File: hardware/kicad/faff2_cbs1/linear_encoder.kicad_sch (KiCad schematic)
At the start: 0 parts

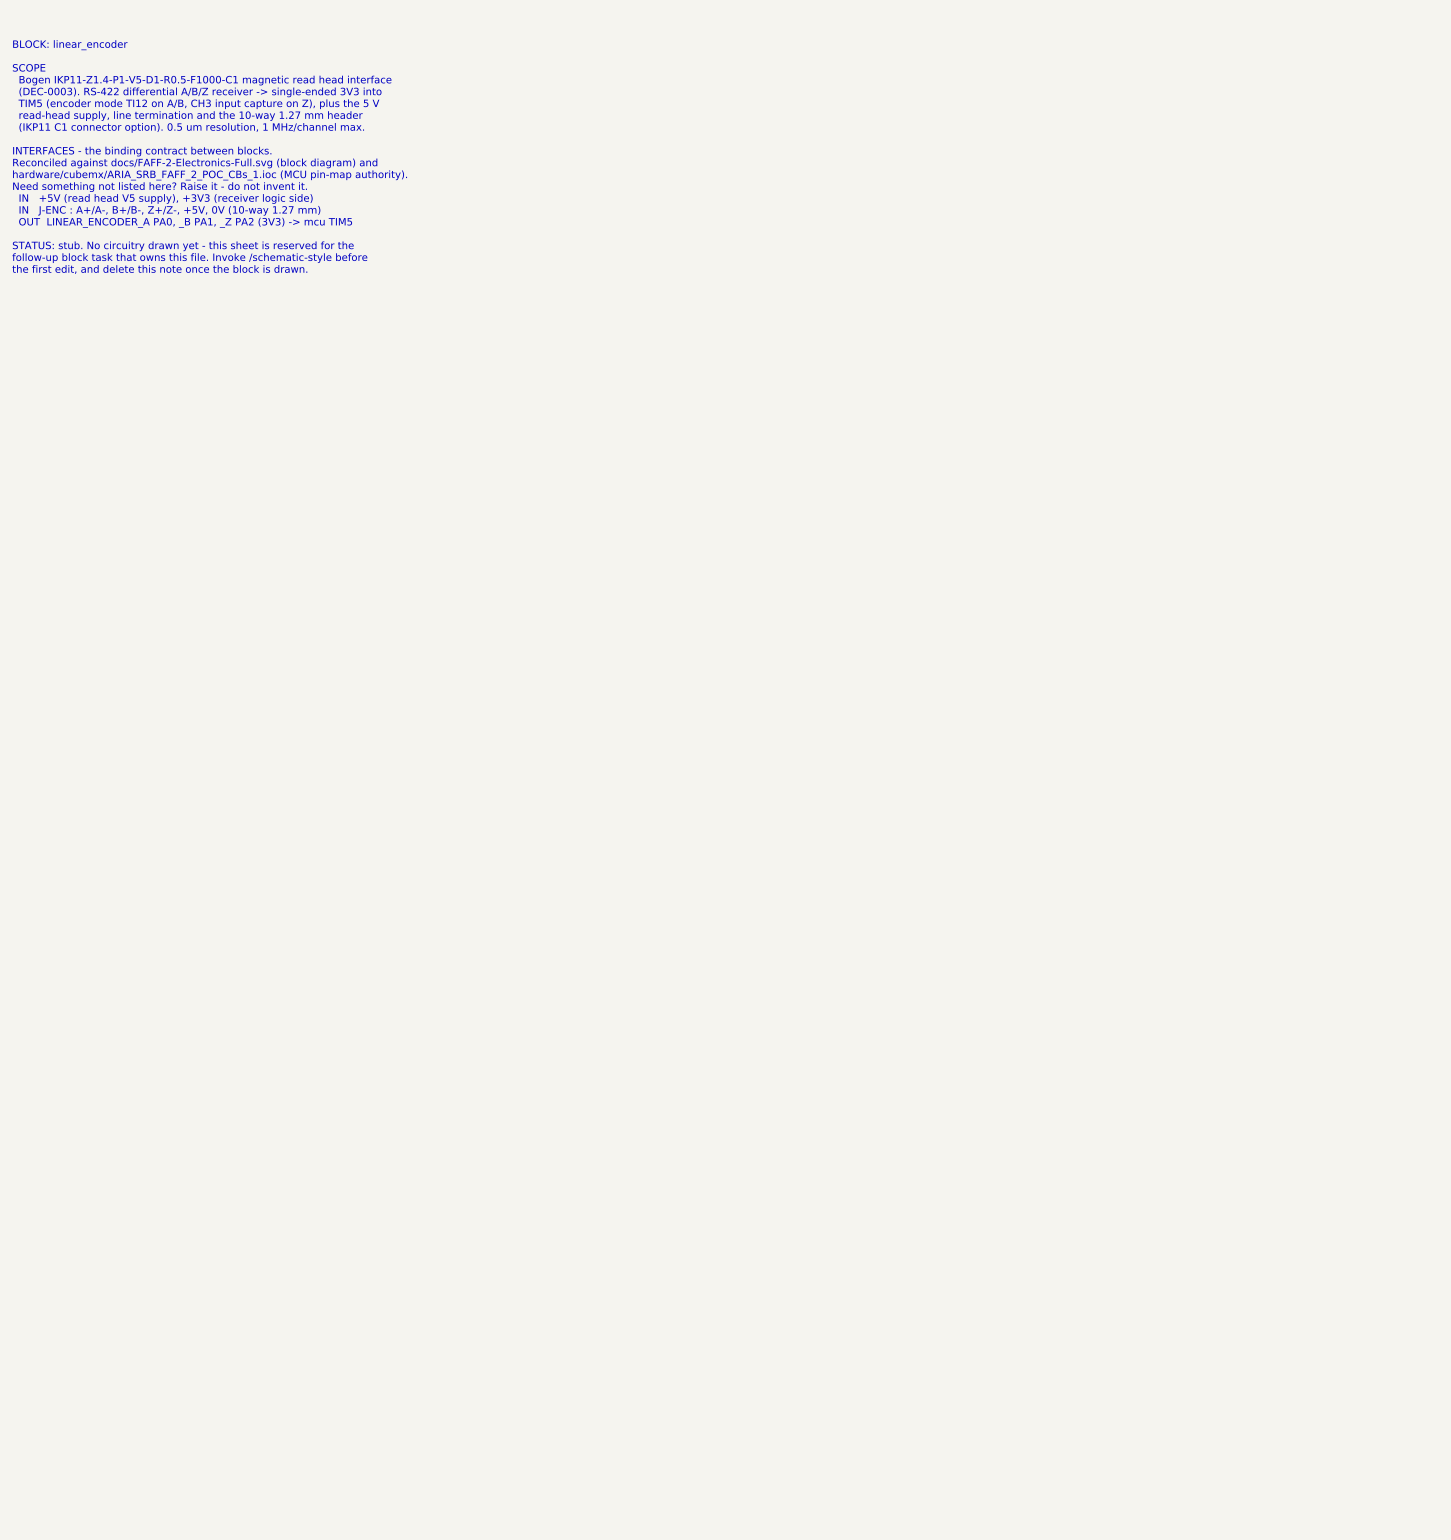
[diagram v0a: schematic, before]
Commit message: periph: draw linear_encoder, nvm_calibration and ui_io
Three peripheral block sheets for FAFF 2 CBs_1, drawn to the
/schematic-style house rules on the KiCad 9 A3 frame.

linear_encoder (REQ-PS-01..10, REQ-AR-07, DEC-0003)
  Bogen IKP11-Z1.4-P1-V5-D1-R0.5-F1000-C1 read head on two parallel
  connectors - a 10-way 0.5 mm FFC (J601, the stock Bogen cable) and a
  2x5 1.27 mm header (J602, the REQ-PS-09 alternative and the quadrature
  injection point).  AM26LV32 quad RS-422 receiver on 3V3 gives native
  3V3 outputs into TIM5; 120 R per pair, with a mid-rail reference and
  three links that switch the block to single-ended / TTL for a D3 head
  or bench injection.  Filtered 5 V read-head supply with its own
  current break, and test points on the receiver outputs.

nvm_calibration (REQ-EL-08, REQ-AR-11)
  24FC16T-I/OT 16 kbit I2C EEPROM on I2C1, 4k7 pull-ups on removable
  links, in-line solder bridges to take the device off the bus, and a
  write-protect network that resolves OQ-06 without spending an MCU pin.

ui_io (REQ-EL-05/06/09, REQ-CC-06, REQ-SF-01/02/05, DEC-0012)
  Status LEDs, two buttons with an external-button connector for the
  REQ-CC-06 homing trigger, a buffered 50 ohm source-terminated SMA
  SYNC output from TIM15_CH1, and normally-closed end-of-stroke limit
  switches whose two healthy-limit nodes are ANDed into LIMIT_nBRK for
  the TIM1_BKIN2 hardware kill.

References are allocated per sheet from the root page number (6xx, 8xx,
9xx) so the parallel block sheets cannot collide.

Datasheets fetched and committed for the parts selected here.

Co-Authored-By: Claude Opus 5 <noreply@anthropic.com>
Claude-Session: https://claude.ai/code/session_01BewsoRxMKiykAUhQw3HtBp
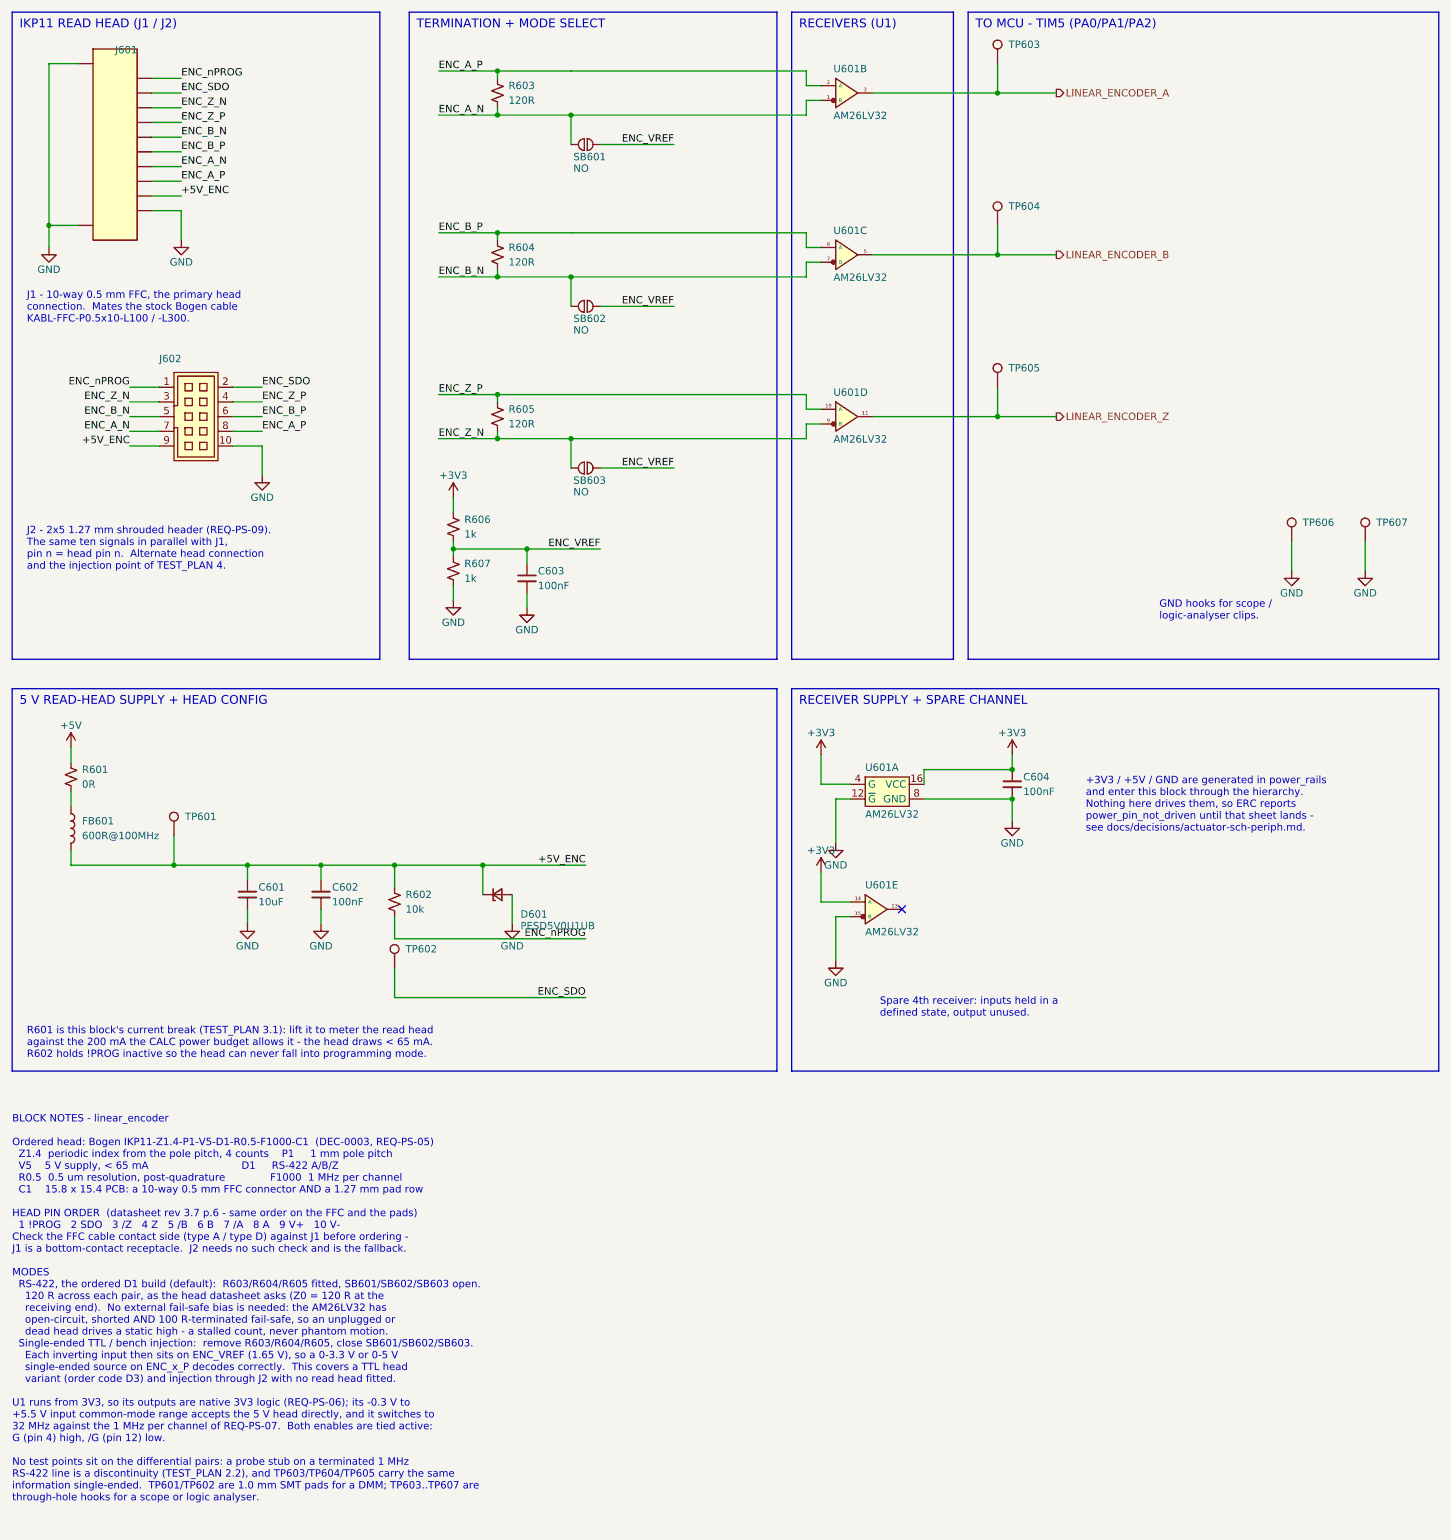
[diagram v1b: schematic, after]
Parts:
- added C601: 10uF, Amodo:C_0805_2012Metric, symbol Amodo_Capacitors:CAP_MLCC_10uF_0805_20%_25V
- added C602, C603, C604: 100nF, Amodo:C_0603_1608Metric, symbol Amodo_Capacitors:CAP_MLCC_100nF_0603_20%_50V
- added D601: PESD5V0U1UB, Amodo:SC-79 (SOD523), symbol Amodo_Diodes:PESD5V0U1UB
- added FB601: 600R@100MHz, Amodo:R_0603_1608Metric, symbol Amodo_Inductors:FB_SMD_600R_0603
- added J601: FH12-10S-0.5SH(55), Amodo:FH12-10S-0.5SH(55), symbol Amodo_Connectors:FH12-10S-0.5SH(55)
- added J602: FTSH-105-01-L-DV-K-TR, Amodo:FTSH-105-01-L-DV-K-TR, symbol Amodo_Connectors:FTSH-105-01-L-DV-K-TR
- added R601: 0R, Amodo:R_0603_1608Metric, symbol Amodo_Resistors:RES_TF_0R_0603
- added R602: 10k, Amodo:R_0603_1608Metric, symbol Amodo_Resistors:RES_TF_10k_0603
- added R603, R604, R605: 120R, Amodo:R_0603_1608Metric, symbol Amodo_Resistors:RES_TF_120R_0603
- added R606, R607: 1k, Amodo:R_0603_1608Metric, symbol Amodo_Resistors:RES_TF_1k_0603
- added SB601, SB602, SB603: NO, Amodo:SOLDER_JUMPER_NO, symbol Amodo_Resistors:JUMPER_SOLDERABLE_NO
- added TP601, TP602: TestPoint, Amodo:TestPoint_Pad_D1.0mm, symbol Amodo_Connectors:TestPoint
- added TP603, TP604, TP605, TP606, TP607: TestPoint, Amodo:KeystoneMiniatureTestLoop, symbol Amodo_Connectors:TestPointHook
- added U601: AM26LV32, symbol Amodo_Digital_ICs:AM26LS32Ax
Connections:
- new net: FB601.1, R601.2
- new net +3V3: C604.1, R606.1, U601.14 (A), U601.16 (VCC), U601.4 (G)
- new net +5V: R601.1
- new net +5V_ENC: C601.1, C602.1, D601.1 (K), FB601.2, J601.9, J602.9 (Pin_9), R602.1, TP601.1
- new net ENC_A_N: J601.7, J602.7 (Pin_7), R603.2, SB601.1, U601.1 (B)
- new net ENC_A_P: J601.8, J602.8 (Pin_8), R603.1, U601.2 (A)
- new net ENC_B_N: J601.5, J602.5 (Pin_5), R604.2, SB602.1, U601.7 (B)
- new net ENC_B_P: J601.6, J602.6 (Pin_6), R604.1, U601.6 (A)
- new net ENC_SDO: J601.2, J602.2 (Pin_2), TP602.1
- new net ENC_VREF: C603.1, R606.2, R607.1, SB601.2, SB602.2, SB603.2
- new net ENC_Z_N: J601.3, J602.3 (Pin_3), R605.2, SB603.1, U601.9 (B)
- new net ENC_Z_P: J601.4, J602.4 (Pin_4), R605.1, U601.10 (A)
- new net ENC_nPROG: J601.1, J602.1 (Pin_1), R602.2
- new net GND: C601.2, C602.2, C603.2, C604.2, D601.2 (A), J601.10, J601.11, J601.12, J602.10 (Pin_10), R607.2, TP606.1, TP607.1, U601.12 (~{G}), U601.15 (B), U601.8 (GND)
- new net LINEAR_ENCODER_A: TP603.1, U601.3
- new net LINEAR_ENCODER_B: TP604.1, U601.5
- new net LINEAR_ENCODER_Z: TP605.1, U601.11
- no-connect marks 0 -> 1
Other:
- note added: "+3V3 / +5V / GND are generated in power_rails and enter this block through the hierarchy. Nothing here drives them, so ERC reports power_pin_not_driven until that sheet lands - see docs/decisions/actuator-sch-periph.md."
- note added: "5 V READ-HEAD SUPPLY + HEAD CONFIG"
- note added: "BLOCK NOTES - linear_encoder Ordered head: Bogen IKP11-Z1.4-P1-V5-D1-R0.5-F1000-C1 (DEC-0003, REQ-PS-05) Z1.4 periodic index from the pole pitch, 4 counts P1 1 mm pole pitch V5 5 V supply, < 65 mA D1 RS-422 A/B/Z R0.5 0.5 um resolution, post-quadrature F1000 1 MHz per channel C1 15.8 x 15.4 PCB: a 10-way 0.5 mm FFC connector AND a 1.27 mm pad row HEAD PIN ORDER (datasheet rev 3.7 p.6 - same order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"
- note added: "GND hooks for scope / logic-analyser clips."
- note added: "IKP11 READ HEAD (J1 / J2)"
- note added: "J1 - 10-way 0.5 mm FFC, the primary head connection. Mates the stock Bogen cable KABL-FFC-P0.5x10-L100 / -L300."
- note added: "J2 - 2x5 1.27 mm shrouded header (REQ-PS-09). The same ten signals in parallel with J1, pin n = head pin n. Alternate head connection and the injection point of TEST_PLAN 4."
- note added: "R601 is this block's current break (TEST_PLAN 3.1): lift it to meter the read head against the 200 mA the CALC power budget allows it - the head draws < 65 mA. R602 holds !PROG inactive so the head can never fall into programming mode."
- note added: "RECEIVER SUPPLY + SPARE CHANNEL"
- note added: "RECEIVERS (U1)"
- note added: "Spare 4th receiver: inputs held in a defined state, output unused."
- note added: "TERMINATION + MODE SELECT"
- note added: "TO MCU - TIM5 (PA0/PA1/PA2)"
- note removed: "BLOCK: linear_encoder SCOPE Bogen IKP11-Z1.4-P1-V5-D1-R0.5-F1000-C1 magnetic read head interface (DEC-0003). RS-422 differential A/B/Z receiver -> single-ended 3V3 into TIM5 (encoder mode TI12 on A/B, CH3 input capture on Z), plus the 5 V read-head supply, line termination and the 10-way 1.27 mm header (IKP11 C1 connector option). 0.5 um resolution, 1 MHz/channel max. INTERFACES - the binding con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"

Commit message: periph: move the FH12-10S part into project-local libraries
AmodoKiCadLib is read-only (captain rule), so the one new part this
block needed lives in the project instead:

  hardware/kicad/faff2_cbs1/faff2_periph.kicad_sym   symbol
  hardware/kicad/faff2_cbs1/faff2.pretty/            footprint

with sym-lib-table and fp-lib-table entries resolved through
${KIPRJMOD}.  faff2.pretty is shared with motor_drive; distinct
.kicad_mod filenames do not collide.

linear_encoder.kicad_sch now references faff2_periph:FH12-10S-0.5SH(55)
with footprint faff2:FH12-10S-0.5SH(55); no stale Amodo reference to the
part remains.  The earlier edits to Amodo_Connectors.kicad_sym and
Amodo.pretty were reverted with targeted commands and verified clean.

ERC unchanged: 0 warnings, and no lib_symbol_issues or
footprint_link_issues, so both project-local tables resolve.

Co-Authored-By: Claude Opus 5 <noreply@anthropic.com>
Claude-Session: https://claude.ai/code/session_01BewsoRxMKiykAUhQw3HtBp
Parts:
- J601: footprint Amodo:FH12-10S-0.5SH(55) -> faff2:FH12-10S-0.5SH(55); symbol Amodo_Connectors:FH12-10S-0.5SH(55) -> faff2_periph:FH12-10S-0.5SH(55)
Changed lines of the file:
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@@
 	)
 	(symbol
-		(lib_id "Amodo_Connectors:FH12-10S-0.5SH(55)")
+		(lib_id "faff2_periph:FH12-10S-0.5SH(55)")
 		(at 33.0200 43.1800 0)
 		(unit 1)
@@
 			)
 		)
-		(property "Footprint" "Amodo:FH12-10S-0.5SH(55)"
+		(property "Footprint" "faff2:FH12-10S-0.5SH(55)"
 			(at 54.6100 138.1000 0)
 			(effects

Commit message: integrate: RTA0040B land pattern for the DRV8323S, and two footprints assigned
The DRV8323S footprint was owed since the motor block landed: SLVSDJ3D
ships the RTV0032E and RGZ0048A package drawings but not RTA0040's, so
there was nothing to draw from.

Found it: TI drawing 4219112/A (07/2018), RTA0040B, in the DRV8353 data
sheet pp.98-100. Committed as
datasheets/DRV832x_RTA0040B_package_4219112A.pdf so the next reader does
not repeat the hunt. Set beside TI 4219052/A (RHA0040B, from
msp430g2755.pdf p.72), the two give an identical outline and an identical
land pattern - 6.1/5.9 body, 36X 0.5 pitch, 2X 4.5 terminal span, 40X
0.5/0.3 terminal length, 4.15+/-0.1 exposed pad, land 40X (0.6)x(0.22)
inside (5.8), stencil 9X (1.17) on (1.37) - and differ only in package
height, 0.8 mm WQFN against 1.0 mm VQFN.

So KiCad 9's official Texas_RHA0040B footprint is a dimension-verified
base, which is what pcb-layout-style allows: its perimeter pads,
silkscreen, fab outline and courtyard are reproduced in
faff2.pretty/Texas_RTA0040B_WQFN-40-1EP_6x6mm_P0.5mm_EP4.15x4.15mm, with
two deliberate departures - TI's own 9X (1.17) on (1.37) stencil
apertures (71.5% coverage against TI's stated 71%), and IPC-nominal
perimeter pads kept as a superset of TI's own tighter land, matching the
house QFN footprints in Amodo.pretty and leaving an inspectable toe.

Geometry asserted programmatically: 40 pads, ten a side, 0.5 mm pitch,
4.5 mm span, row offset 2.9375, EP 4.15 square, pin 1 the top pad of the
left column - the anticlockwise numbering of SLVSDJ3D figure 6-6, which
the symbol's own 41 pins (pin 41 = PAD) match name for name.

U601 (AM26LV32, linear_encoder) also had no footprint: the house
AM26LS32Ax symbol carries none. Assigned Amodo:SOIC-16-N, the reviewed
house land for the 3.9x9.9 mm D package the part's mpn names. Every one
of the 409 components now resolves to a footprint, and all 51 distinct
footprints resolve to a file in Amodo.pretty or faff2.pretty.

ERC still 0/0 at seve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
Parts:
- U601: footprint (none) -> Amodo:SOIC-16-N
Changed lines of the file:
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@@
 			)
 		)
-		(property "Footprint" ""
+		(property "Footprint" "Amodo:SOIC-16-N"
 			(at 157.4800 31.7500 0)
 			(effects
@@
 			)
 		)
-		(property "Footprint" ""
+		(property "Footprint" "Amodo:SOIC-16-N"
 			(at 157.4800 59.6900 0)
 			(effects
@@
 			)
 		)
-		(property "Footprint" ""
+		(property "Footprint" "Amodo:SOIC-16-N"
 			(at 157.4800 87.6300 0)
 			(effects
@@
 			)
 		)
-		(property "Footprint" ""
+		(property "Footprint" "Amodo:SOIC-16-N"
 			(at 162.5600 152.4000 0)
 			(effects
@@
 			)
 		)
-		(property "Footprint" ""
+		(property "Footprint" "Amodo:SOIC-16-N"
 			(at 162.5600 172.7200 0)
 			(effects
